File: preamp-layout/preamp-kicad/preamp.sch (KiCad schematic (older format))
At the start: 0 parts

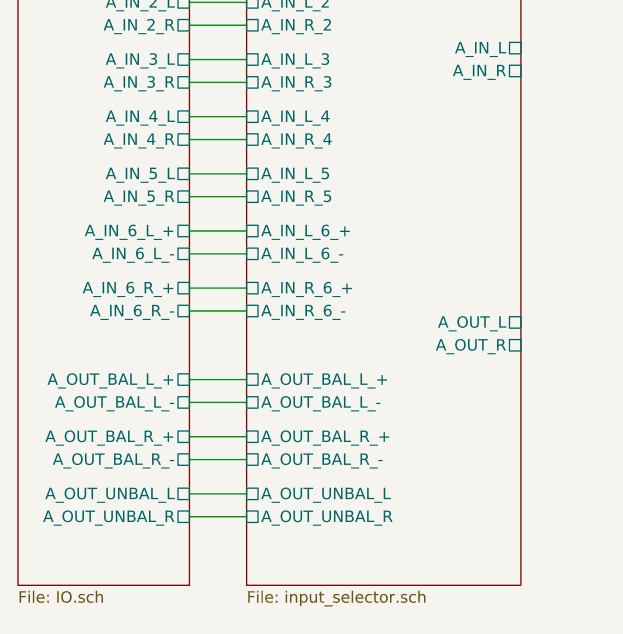
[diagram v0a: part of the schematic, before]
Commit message: BOM skeleton added. gitignore updated to ignore schematic bak files. General work done on the schematic layout.
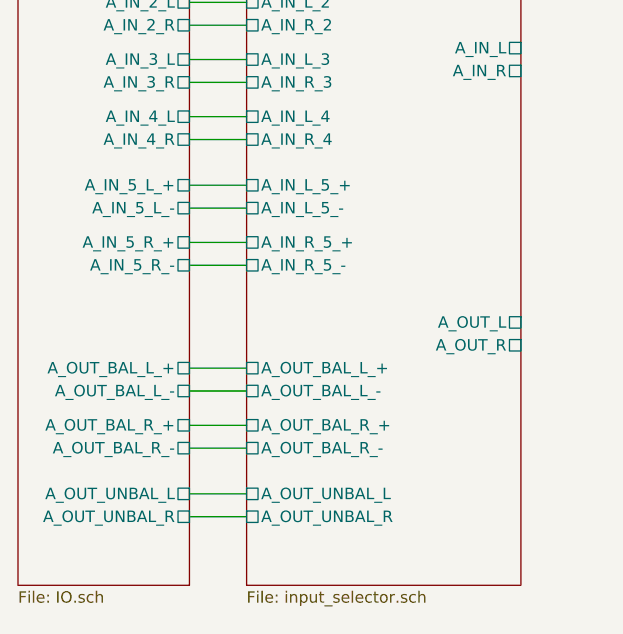
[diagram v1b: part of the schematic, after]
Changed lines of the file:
@@
 EESchema Schematic File Version 4
+LIBS:preamp-cache
 EELAYER 30 0
 EELAYER END
@@
 F6 "A_IN_L_1" U L 2000 1150 50
 F7 "A_IN_R_1" U L 2000 1250 50
-F8 "A_IN_L_6_+" U L 2000 2400 50
-F9 "A_IN_L_6_-" U L 2000 2500 50
-F10 "A_IN_R_6_+" U L 2000 2650 50
-F11 "A_IN_R_6_-" U L 2000 2750 50
-F12 "A_OUT_UNBAL_R" U L 2000 3650 50
-F13 "A_OUT_UNBAL_L" U L 2000 3550 50
-F14 "A_OUT_BAL_L_-" U L 2000 3150 50
-F15 "A_OUT_BAL_L_+" U L 2000 3050 50
-F16 "A_OUT_BAL_R_-" U L 2000 3400 50
-F17 "A_OUT_BAL_R_+" U L 2000 3300 50
-F18 "A_IN_L_2" U L 2000 1400 50
-F19 "A_IN_R_2" U L 2000 1500 50
-F20 "A_IN_L_3" U L 2000 1650 50
-F21 "A_IN_R_3" U L 2000 1750 50
-F22 "A_IN_L_4" U L 2000 1900 50
-F23 "A_IN_R_4" U L 2000 2000 50
-F24 "A_IN_L_5" U L 2000 2150 50
-F25 "A_IN_R_5" U L 2000 2250 50
+F8 "A_OUT_UNBAL_R" U L 2000 3650 50
+F9 "A_OUT_UNBAL_L" U L 2000 3550 50
+F10 "A_OUT_BAL_L_-" U L 2000 3100 50
+F11 "A_OUT_BAL_L_+" U L 2000 3000 50
+F12 "A_OUT_BAL_R_-" U L 2000 3350 50
+F13 "A_OUT_BAL_R_+" U L 2000 3250 50
+F14 "A_IN_L_2" U L 2000 1400 50
+F15 "A_IN_R_2" U L 2000 1500 50
+F16 "A_IN_L_3" U L 2000 1650 50
+F17 "A_IN_R_3" U L 2000 1750 50
+F18 "A_IN_L_4" U L 2000 1900 50
+F19 "A_IN_R_4" U L 2000 2000 50
+F20 "A_IN_L_5_+" U L 2000 2200 50
+F21 "A_IN_L_5_-" U L 2000 2300 50
+F22 "A_IN_R_5_+" U L 2000 2450 50
+F23 "A_IN_R_5_-" U L 2000 2550 50
 $EndSheet
 $Sheet
@@
 F8 "A_IN_4_L" U R 1750 1900 50
 F9 "A_IN_4_R" U R 1750 2000 50
-F10 "A_IN_5_L" U R 1750 2150 50
-F11 "A_IN_5_R" U R 1750 2250 50
-F12 "A_IN_6_L_-" U R 1750 2500 50
-F13 "A_IN_6_L_+" U R 1750 2400 50
-F14 "A_IN_6_R_-" U R 1750 2750 50
-F15 "A_IN_6_R_+" U R 1750 2650 50
-F16 "A_OUT_BAL_L_-" U R 1750 3150 50
-F17 "A_OUT_BAL_L_+" U R 1750 3050 50
-F18 "A_OUT_BAL_R_-" U R 1750 3400 50
-F19 "A_OUT_BAL_R_+" U R 1750 3300 50
-F20 "A_OUT_UNBAL_L" U R 1750 3550 50
-F21 "A_OUT_UNBAL_R" U R 1750 3650 50
+F10 "A_OUT_BAL_L_-" U R 1750 3100 50
+F11 "A_OUT_BAL_L_+" U R 1750 3000 50
+F12 "A_OUT_BAL_R_-" U R 1750 3350 50
+F13 "A_OUT_BAL_R_+" U R 1750 3250 50
+F14 "A_OUT_UNBAL_L" U R 1750 3550 50
+F15 "A_OUT_UNBAL_R" U R 1750 3650 50
+F16 "A_IN_5_L_-" U R 1750 2300 50
+F17 "A_IN_5_L_+" U R 1750 2200 50
+F18 "A_IN_5_R_-" U R 1750 2550 50
+F19 "A_IN_5_R_+" U R 1750 2450 50
 $EndSheet
 Wire Wire Line
@@
 	1750 2000 2000 2000
 Wire Wire Line
-	1750 2150 2000 2150
+	1750 2200 2000 2200
 Wire Wire Line
-	1750 2250 2000 2250
+	1750 2300 2000 2300
 Wire Wire Line
-	1750 2400 2000 2400
+	1750 2450 2000 2450
 Wire Wire Line
-	1750 2500 2000 2500
+	1750 2550 2000 2550
 Wire Wire Line
-	1750 2650 2000 2650
+	1750 3000 2000 3000
 Wire Wire Line
-	1750 2750 2000 2750
+	1750 3100 2000 3100
 Wire Wire Line
-	1750 3050 2000 3050
+	1750 3250 2000 3250
 Wire Wire Line
-	1750 3150 2000 3150
-Wire Wire Line
-	1750 3300 2000 3300
-Wire Wire Line
-	1750 3400 2000 3400
+	1750 3350 2000 3350
 Wire Wire Line
 	1750 3550 2000 3550

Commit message: IO layout cleanup
Changed location of bal/unbal buffers from selector board to daughter board. Generalized IO PCB to accept daughter boards, not specific to connector type or bal/unbal. The idea is that as many unbalanced RCAs can be populated on the main IO board as desired and jumper cables can also be added to daughter boards as needed for different kinds of IO, but the interface to the selector board does not need to change to allow this.
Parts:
- added R? (x8): 10K, symbol Device:R
- added R? (x2): 100R, symbol Device:R
- added U? (x3): TL072, symbol Amplifier_Operational:TL072
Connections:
- new net: R?.1, R?.1, U?.3 (+)
- new net: R?.1, R?.2, U?.1
- new net: R?.1, R?.2, U?.2 (-)
- new net: R?.1, R?.1, U?.5 (+)
- new net: R?.1, R?.2, U?.7
- new net: R?.1, R?.2, U?.6 (-)
- new net +15V: U?.8 (V+)
- new net -15V: U?.4 (V-)
- new net A_OUT_L: R?.2
- new net A_OUT_R: R?.2
- new net A_OUT_UNBAL_L: R?.1
- new net A_OUT_UNBAL_R: R?.1
- new net GNDS: R?.2, R?.2, R?.2, R?.2

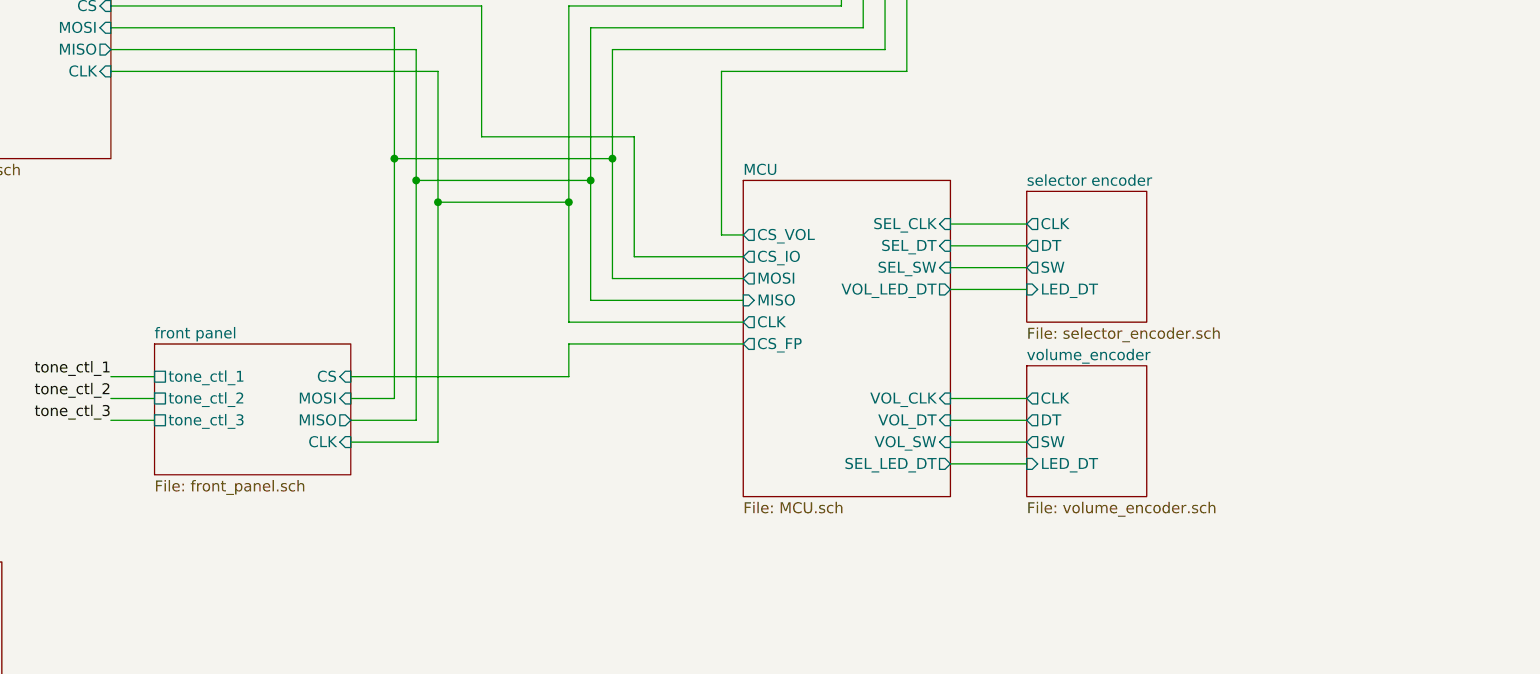
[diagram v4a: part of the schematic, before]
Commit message: Encoder, LED, front panel update
Removed hierarchical sheets for encoders, moved encoders to main sheet. Added switches for output select on front panel sheet. Added LEDs on front panel sheet but only as a symbol, only two instances currently present. Added LED data line between MCU and front panel.
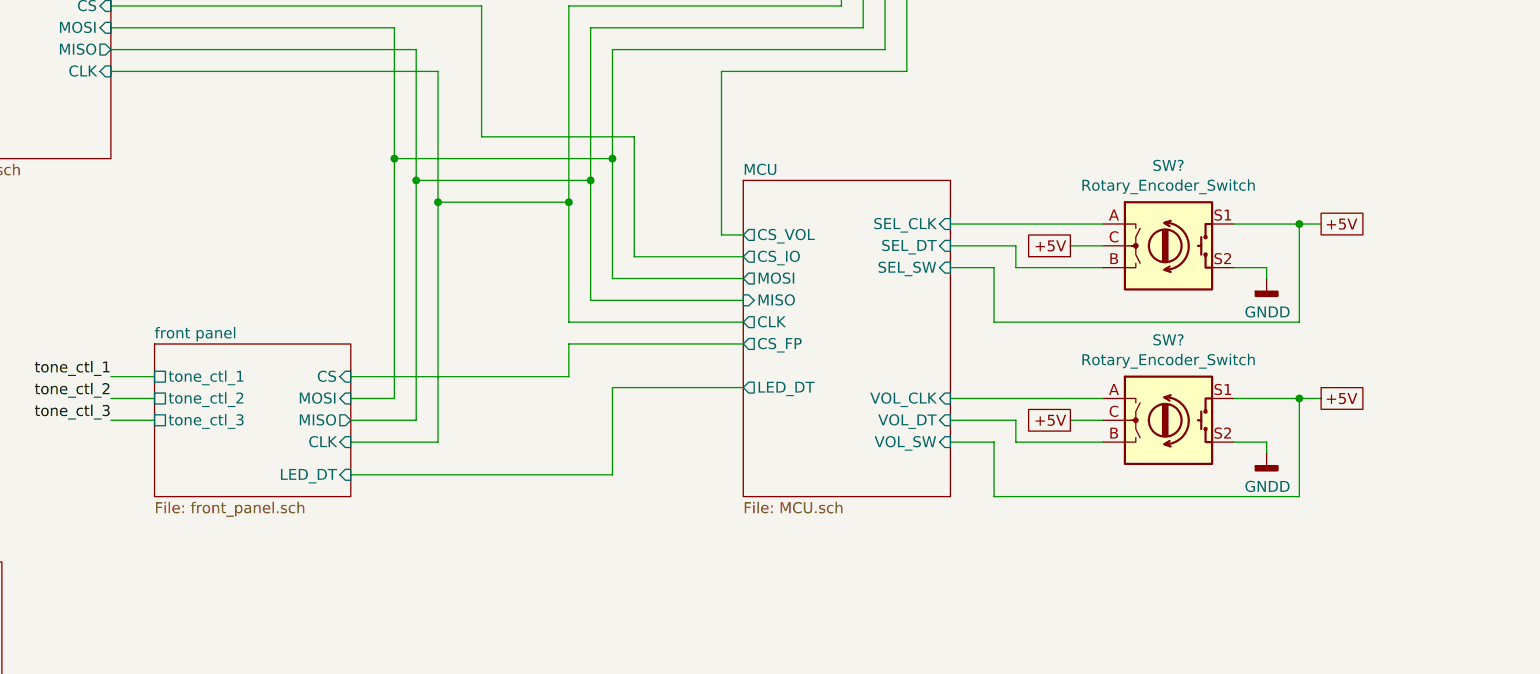
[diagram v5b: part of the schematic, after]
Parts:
- added SW? (x2): Rotary_Encoder_Switch, symbol Device:Rotary_Encoder_Switch
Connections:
- net MCU/SEL_CLK: now also SW?.A
- net MCU/SEL_DT: now also SW?.B
- net MCU/VOL_CLK: now also SW?.A
- net MCU/VOL_DT: now also SW?.B
- new net +5V: SW?.C, SW?.C, SW?.S1, SW?.S1
- new net GNDD: SW?.S2, SW?.S2
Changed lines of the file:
@@
 $Descr A4 11693 8268
 encoding utf-8
-Sheet 1 14
+Sheet 1 12
 Title ""
 Date ""
@@
 	4850 4600 5050 4600
 $Sheet
-S 5050 4450 900  600
+S 5050 4450 900  700
 U 5E5ECAAE
 F0 "front panel" 50
@@
 F7 "tone_ctl_2" U L 5050 4700 50
 F8 "tone_ctl_3" U L 5050 4800 50
-$EndSheet
-Wire Wire Line
-	8700 5000 9050 5000
-Wire Wire Line
-	8700 4900 9050 4900
-Wire Wire Line
-	8700 4800 9050 4800
-Wire Wire Line
-	8700 4700 9050 4700
-Wire Wire Line
-	8700 4200 9050 4200
-Wire Wire Line
-	8700 4100 9050 4100
-Wire Wire Line
-	8700 4000 9050 4000
-Wire Wire Line
-	8700 3900 9050 3900
-$Sheet
-S 9050 3750 550  600
-U 63AE120F
-F0 "selector encoder" 50
-F1 "selector_encoder.sch" 50
-F2 "CLK" O L 9050 3900 50
-F3 "DT" O L 9050 4000 50
-F4 "SW" O L 9050 4100 50
-F5 "LED_DT" I L 9050 4200 50
-$EndSheet
-$Sheet
-S 9050 4550 550  600
-U 63AE11F4
-F0 "volume_encoder" 50
-F1 "volume_encoder.sch" 50
-F2 "CLK" O L 9050 4700 50
-F3 "DT" O L 9050 4800 50
-F4 "SW" O L 9050 4900 50
-F5 "LED_DT" I L 9050 5000 50
+F9 "LED_DT" I R 5950 5050 50
 $EndSheet
 $Sheet
@@
 F10 "VOL_DT" I R 8700 4800 50
 F11 "VOL_SW" I R 8700 4900 50
-F12 "VOL_LED_DT" O R 8700 4200 50
-F13 "SEL_LED_DT" O R 8700 5000 50
-F14 "CS_FP" O L 7750 4450 50
-F15 "CS_VOL" O L 7750 3950 50
+F12 "CS_FP" O L 7750 4450 50
+F13 "CS_VOL" O L 7750 3950 50
+F14 "LED_DT" O L 7750 4650 50
 $EndSheet
 Wire Wire Line
@@
 Wire Wire Line
 	6350 3200 6350 3800
+$Comp
+L Device:Rotary_Encoder_Switch SW?
+U 1 1 5E975BA4
+P 9700 4000
+AR Path="/63AE120F/5E975BA4" Ref="SW?"  Part="1"
+AR Path="/5E975BA4" Ref="SW?"  Part="1"
+F 0 "SW?" H 9700 4367 50  0000 C CNN
+F 1 "Rotary_Encoder_Switch" H 9700 4276 50  0000 C CNN
+F 2 "" H 9550 4160 50  0001 C CNN
+F 3 "~" H 9700 4260 50  0001 C CNN
+	1    9700 4000
+	1    0    0    -1
+$EndComp
+$Comp
+L power:GNDD #PWR?
+U 1 1 5E975BAA
+P 10150 4150
+AR Path="/63AE120F/5E975BAA" Ref="#PWR?"  Part="1"
+AR Path="/5E975BAA" Ref="#PWR?"  Part="1"
+F 0 "#PWR?" H 10150 3900 50  0001 C CNN
+F 1 "GNDD" H 10154 3995 50  0000 C CNN
+F 2 "" H 10150 4150 50  0001 C CNN
+F 3 "" H 10150 4150 50  0001 C CNN
+	1    10150 4150
+	1    0    0    -1
+$EndComp
+Text GLabel 10400 3900 2    50   UnSpc ~ 0
++5V
+Wire Wire Line
+	10000 3900 10300 3900
+Wire Wire Line
+	10000 4100 10150 4100
+Wire Wire Line
+	10150 4100 10150 4150
+Text GLabel 9250 4000 0    50   UnSpc ~ 0
++5V
+Wire Wire Line
+	9250 4000 9400 4000
+Wire Wire Line
+	8700 3900 9400 3900
+Wire Wire Line
+	9000 4100 9000 4000
+Wire Wire Line
+	9000 4000 8700 4000
+Wire Wire Line
+	9000 4100 9400 4100
+Wire Wire Line
+	10300 3900 10300 4350
+Wire Wire Line
+	10300 4350 8900 4350
+Wire Wire Line
+	8900 4350 8900 4100
+Wire Wire Line
+	8900 4100 8700 4100
+$Comp
+L Device:Rotary_Encoder_Switch SW?
+U 1 1 5E9C5C27
+P 9700 4800
+AR Path="/63AE120F/5E9C5C27" Ref="SW?"  Part="1"
+AR Path="/5E9C5C27" Ref="SW?"  Part="1"
+F 0 "SW?" H 9700 5167 50  0000 C CNN
+F 1 "Rotary_Encoder_Switch" H 9700 5076 50  0000 C CNN
+F 2 "" H 9550 4960 50  0001 C CNN
+F 3 "~" H 9700 5060 50  0001 C CNN
+	1    9700 4800
+	1    0    0    -1
+$EndComp
+$Comp
+L power:GNDD #PWR?
+U 1 1 5E9C5C31
+P 10150 4950
+AR Path="/63AE120F/5E9C5C31" Ref="#PWR?"  Part="1"
+AR Path="/5E9C5C31" Ref="#PWR?"  Part="1"
+F 0 "#PWR?" H 10150 4700 50  0001 C CNN
+F 1 "GNDD" H 10154 4795 50  0000 C CNN
+F 2 "" H 10150 4950 50  0001 C CNN
+F 3 "" H 10150 4950 50  0001 C CNN
+	1    10150 4950
+	1    0    0    -1
+$EndComp
+Wire Wire Line
+	10000 4700 10300 4700
+Wire Wire Line
+	10000 4900 10150 4900
+Wire Wire Line
+	10150 4900 10150 4950
+Text GLabel 9250 4800 0    50   UnSpc ~ 0
++5V
+Wire Wire Line
+	9250 4800 9400 4800
+Wire Wire Line
+	8700 4700 9400 4700
+Wire Wire Line
+	9000 4900 9000 4800
+Wire Wire Line
+	9000 4800 8700 4800
+Wire Wire Line
+	9000 4900 9400 4900
+Wire Wire Line
+	10300 4700 10300 5150
+Wire Wire Line
+	10300 5150 8900 5150
+Wire Wire Line
+	8900 5150 8900 4900
+Wire Wire Line
+	8900 4900 8700 4900
+Wire Wire Line
+	10400 3900 10300 3900
+Connection ~ 10300 3900
+Text GLabel 10400 4700 2    50   UnSpc ~ 0
++5V
+Wire Wire Line
+	10400 4700 10300 4700
+Connection ~ 10300 4700
+Wire Wire Line
+	7750 4650 7150 4650
+Wire Wire Line
+	7150 4650 7150 5050
+Wire Wire Line
+	7150 5050 5950 5050
 $EndSCHEMATC

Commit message: Tone Control update
Generated analog tone controls controlled either by pots mounted on the front panel or encoders mounted on the front panel that communicate to the tone control board via SPI.
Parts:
- removed R? (x8): 10K, symbol Device:R
- removed R? (x2): 100R, symbol Device:R
- removed U? (x3): TL072, symbol Amplifier_Operational:TL072
- added R? (x8): 10K, symbol Device:R
- added R? (x2): 100R, symbol Device:R
- added U? (x3): TL072, symbol Amplifier_Operational:TL072
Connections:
- net +15V: now also U?.8 (V+)
- net -15V: now also U?.4 (V-)
- net A_OUT_L: now also R?.2
- net A_OUT_R: now also R?.2
- net A_OUT_UNBAL_L: now also R?.1
- net A_OUT_UNBAL_R: now also R?.1
- net GNDS: now also R?.2, R?.2, R?.2, R?.2
- new net: R?.1, R?.1, U?.3 (+)
- new net: R?.1, R?.2, U?.1
- new net: R?.1, R?.2, U?.2 (-)
- new net: R?.1, R?.1, U?.5 (+)
- new net: R?.1, R?.2, U?.7
- new net: R?.1, R?.2, U?.6 (-)
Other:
- moved on the sheet: SW?

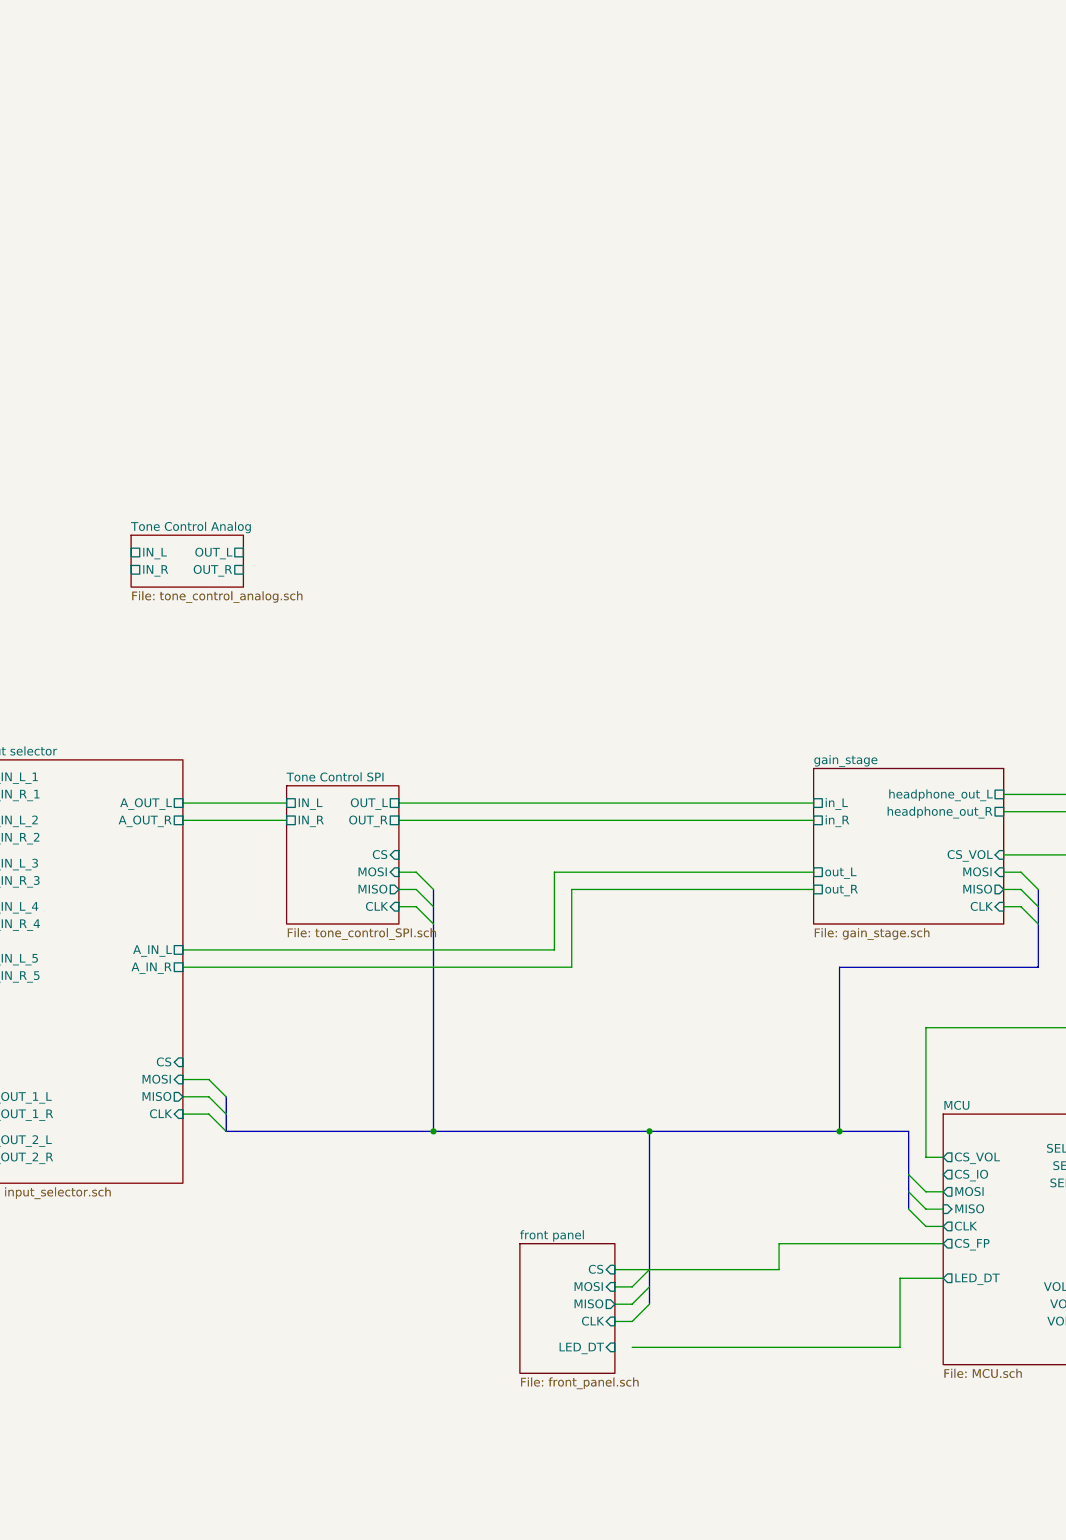
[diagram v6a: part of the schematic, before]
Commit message: Updates
Minor Readme updates.
Schematic:
 - Bus connector lines replaced single wire connectors
 - Title block populated.
 - Power Supply updates.
 - Preliminary Front Panel.
 - Minor MCU work.
 -
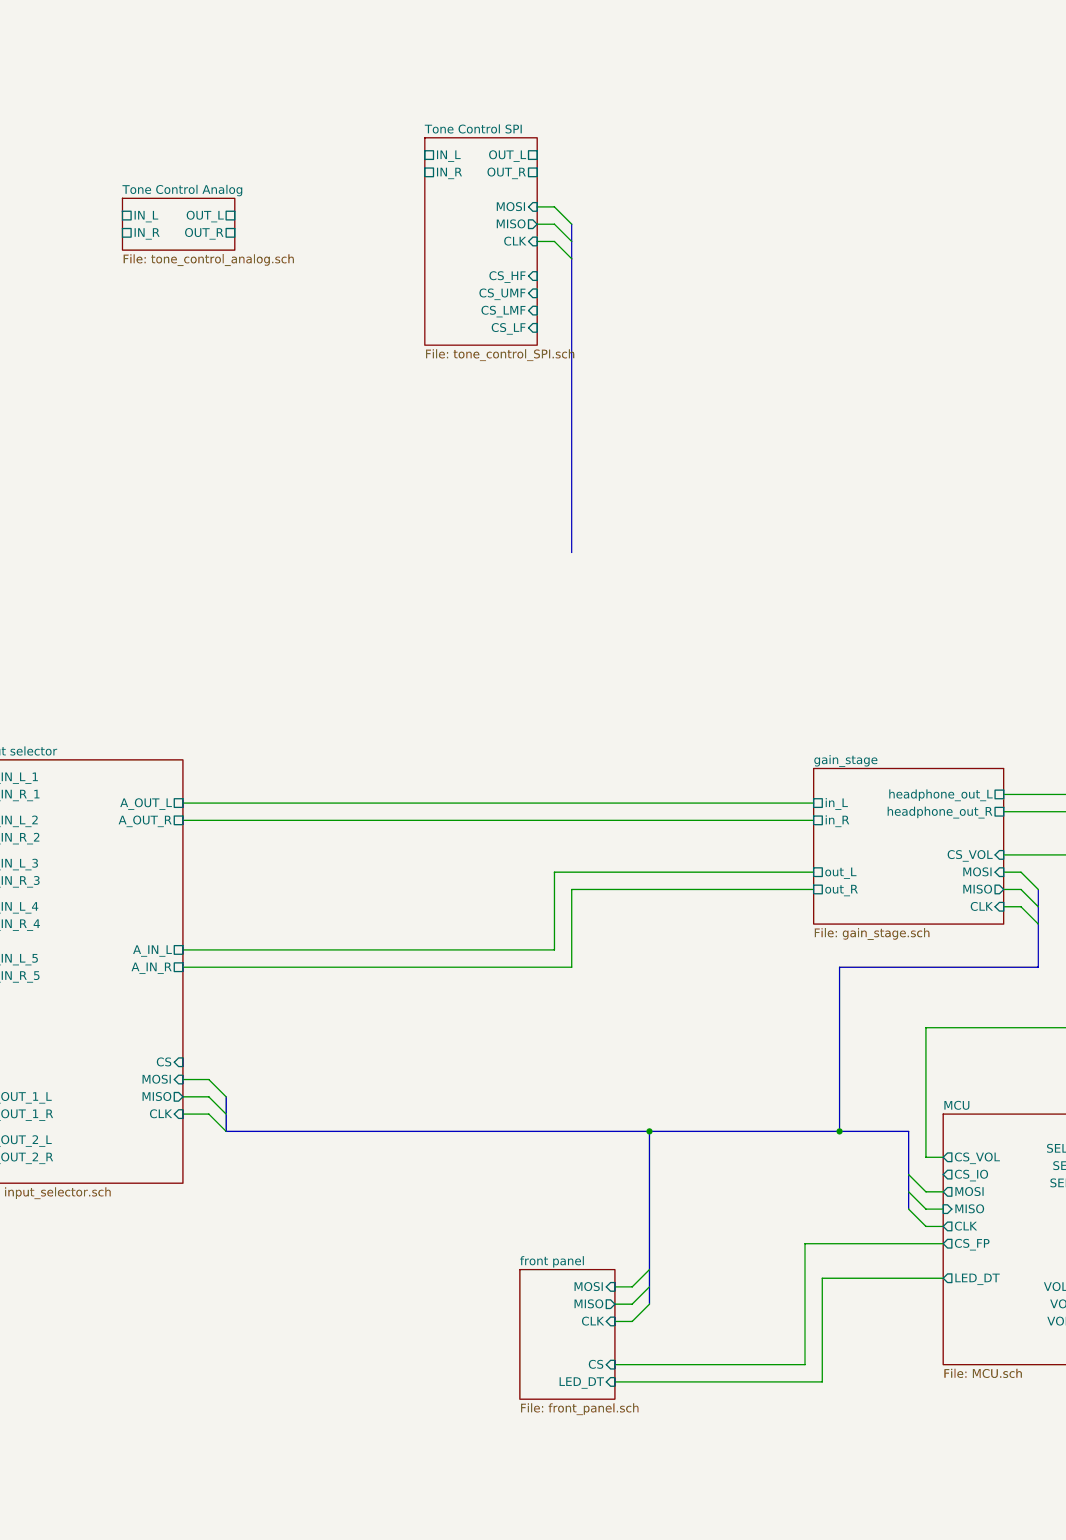
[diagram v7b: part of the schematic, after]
